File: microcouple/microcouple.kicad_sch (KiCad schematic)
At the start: 34 parts, among them J1 Conn_ARM_SWD_TagConnect_TC203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, J2 USB_C_Socket, SW1 ~{RESET}, U1 USBLC6-2SC6, U2 RP2040, X1 12MHz 12pF

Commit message: Finish Silkscreen
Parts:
- C1, C11, C8, C9: footprint Capacitor_SMD:C_0402_1005Metric -> GS_SMD:0402_1005Metric
- C10, C12, C19, C2, C24, C25, C26, C3, C4, C5, C6, C7: footprint Capacitor_SMD:C_0201_0603Metric -> GS_SMD:0201_0603Metric
- D1: footprint LED_SMD:LED_0201_0603Metric -> GS_Optoelectronics:LED_0201_0603Metric
- R1, R2, R3, R6, R7, R8: footprint Resistor_SMD:R_0201_0603Metric -> GS_SMD:0201_0603Metric
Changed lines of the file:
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@@
 			)
 		)
-		(property "Footprint" "Capacitor_SMD:C_0201_0603Metric"
+		(property "Footprint" "GS_SMD:0201_0603Metric"
 			(at 157.1752 36.83 0)
 			(effects
@@
 			)
 		)
-		(property "Footprint" "Resistor_SMD:R_0201_0603Metric"
+		(property "Footprint" "GS_SMD:0201_0603Metric"
 			(at 128.016 61.214 90)
 			(effects
@@
 			)
 		)
-		(property "Footprint" "Capacitor_SMD:C_0201_0603Metric"
+		(property "Footprint" "GS_SMD:0201_0603Metric"
 			(at 38.4048 147.32 0)
 			(effects
@@
 			)
 		)
-		(property "Footprint" "Capacitor_SMD:C_0402_1005Metric"
+		(property "Footprint" "GS_SMD:0402_1005Metric"
 			(at 244.8052 36.83 0)
 			(effects
@@
 			)
 		)
-		(property "Footprint" "Resistor_SMD:R_0201_0603Metric"
+		(property "Footprint" "GS_SMD:0201_0603Metric"
 			(at 218.186 61.214 90)
 			(effects
@@
 			)
 		)
-		(property "Footprint" "Capacitor_SMD:C_0201_0603Metric"
+		(property "Footprint" "GS_SMD:0201_0603Metric"
 			(at 171.1452 36.83 0)
 			(effects
@@
 			)
 		)
-		(property "Footprint" "Capacitor_SMD:C_0201_0603Metric"
+		(property "Footprint" "GS_SMD:0201_0603Metric"
 			(at 165.1 186.9948 0)
 			(effects
@@
 			)
 		)
-		(property "Footprint" "Resistor_SMD:R_0201_0603Metric"
+		(property "Footprint" "GS_SMD:0201_0603Metric"
 			(at 68.326 143.256 90)
 			(effects
@@
 			)
 		)
-		(property "Footprint" "Capacitor_SMD:C_0201_0603Metric"
+		(property "Footprint" "GS_SMD:0201_0603Metric"
 			(at 219.4052 36.83 0)
 			(effects
@@
 			)
 		)
-		(property "Footprint" "Capacitor_SMD:C_0201_0603Metric"
+		(property "Footprint" "GS_SMD:0201_0603Metric"
 			(at 103.8352 134.62 0)
 			(effects
@@
 			)
 		)
-		(property "Footprint" "Resistor_SMD:R_0201_0603Metric"
+		(property "Footprint" "GS_SMD:0201_0603Metric"
 			(at 208.026 61.214 90)
 			(effects
@@
 			)
 		)
-		(property "Footprint" "Capacitor_SMD:C_0201_0603Metric"
+		(property "Footprint" "GS_SMD:0201_0603Metric"
 			(at 119.38 186.9948 0)
 			(effects
@@
 			)
 		)
-		(property "Footprint" "Capacitor_SMD:C_0201_0603Metric"
+		(property "Footprint" "GS_SMD:0201_0603Metric"
 			(at 143.2052 36.83 0)
 			(effects
@@
 			)
 		)
-		(property "Footprint" "Capacitor_SMD:C_0201_0603Metric"
+		(property "Footprint" "GS_SMD:0201_0603Metric"
 			(at 82.2452 134.62 0)
 			(effects
@@
 			)
 		)
-		(property "Footprint" "Capacitor_SMD:C_0201_0603Metric"
+		(property "Footprint" "GS_SMD:0201_0603Metric"
 			(at 270.2052 36.83 0)
 			(effects
@@
 			)
 		)
-		(property "Footprint" "Resistor_SMD:R_0201_0603Metric"
+		(property "Footprint" "GS_SMD:0201_0603Metric"
 			(at 87.376 39.624 90)
 			(effects
@@
 			)
 		)
-		(property "Footprint" "Resistor_SMD:R_0201_0603Metric"
+		(property "Footprint" "GS_SMD:0201_0603Metric"
 			(at 59.944 143.764 90)
 			(effects
@@
 			)
 		)
-		(property "Footprint" "Capacitor_SMD:C_0201_0603Metric"
+		(property "Footprint" "GS_SMD:0201_0603Metric"
 			(at 129.2352 36.83 0)
 			(effects
@@
 			)
 		)
-		(property "Footprint" "Capacitor_SMD:C_0201_0603Metric"
+		(property "Footprint" "GS_SMD:0201_0603Metric"
 			(at 143.51 186.9948 0)
 			(effects
@@
 			)
 		)
-		(property "Footprint" "Capacitor_SMD:C_0402_1005Metric"
+		(property "Footprint" "GS_SMD:0402_1005Metric"
 			(at 115.2652 36.83 0)
 			(effects
@@
 			)
 		)
-		(property "Footprint" "Capacitor_SMD:C_0402_1005Metric"
+		(property "Footprint" "GS_SMD:0402_1005Metric"
 			(at 28.2448 69.85 0)
 			(effects
@@
 			)
 		)
-		(property "Footprint" "Capacitor_SMD:C_0402_1005Metric"
+		(property "Footprint" "GS_SMD:0402_1005Metric"
 			(at 194.0052 36.83 0)
 			(effects
@@
 			)
 		)
-		(property "Footprint" "LED_SMD:LED_0201_0603Metric"
+		(property "Footprint" "GS_Optoelectronics:LED_0201_0603Metric"
 			(at 86.36 31.75 0)
 			(effects

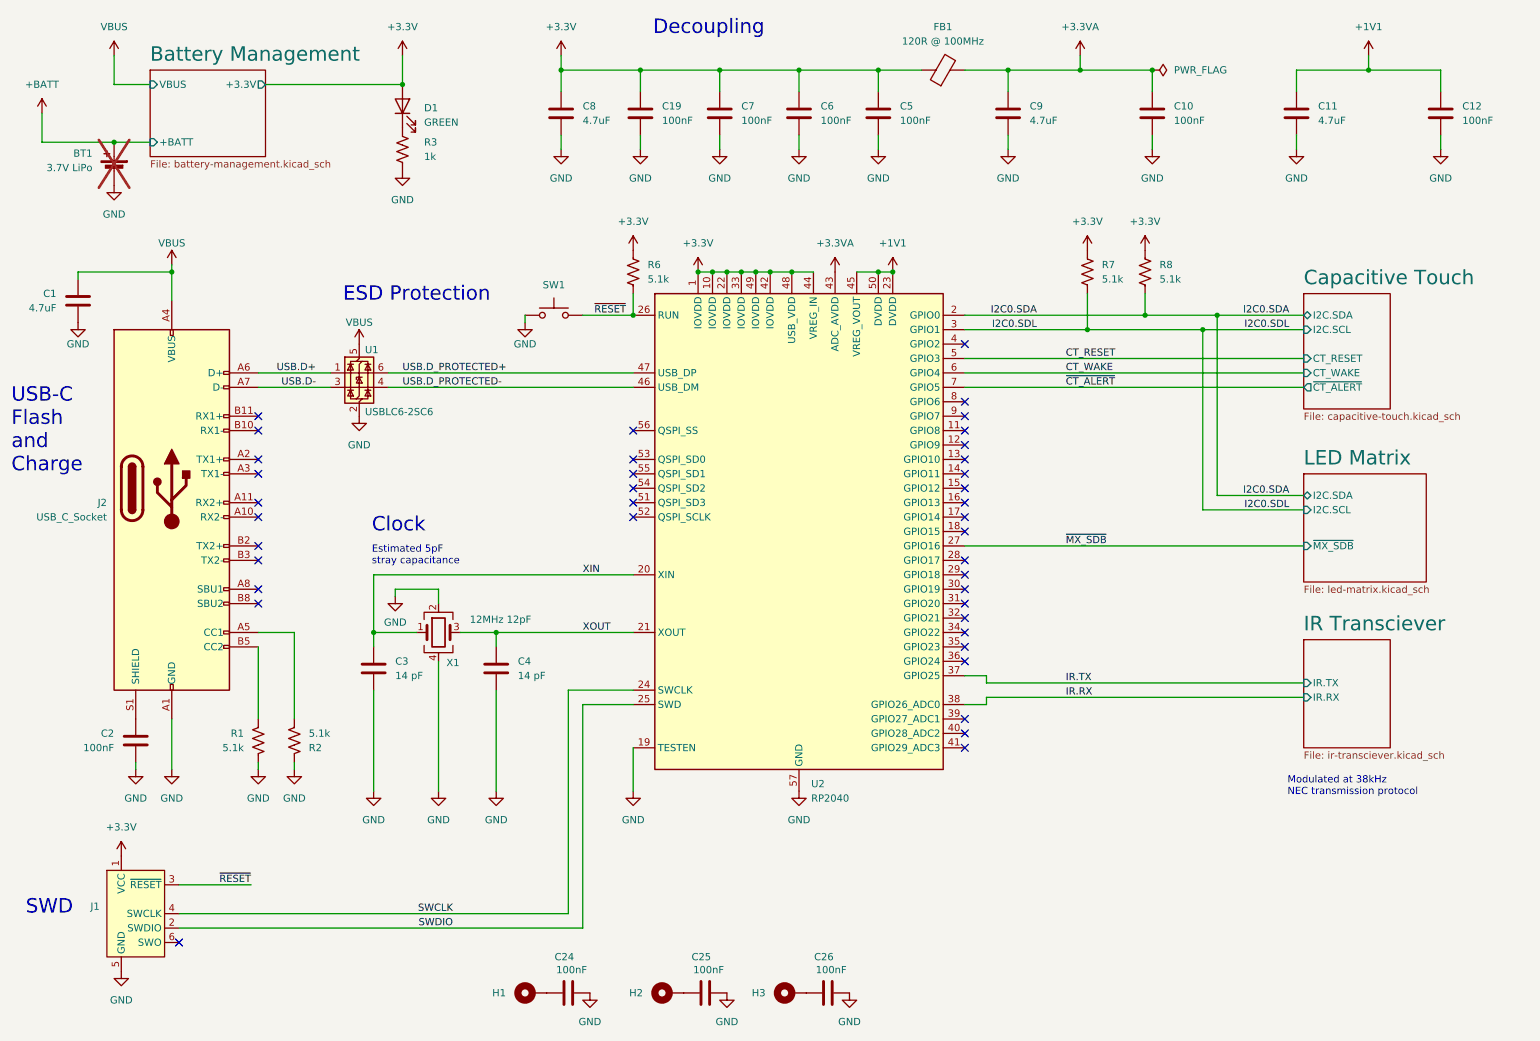
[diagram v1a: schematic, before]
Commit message: Update for JLCPCB
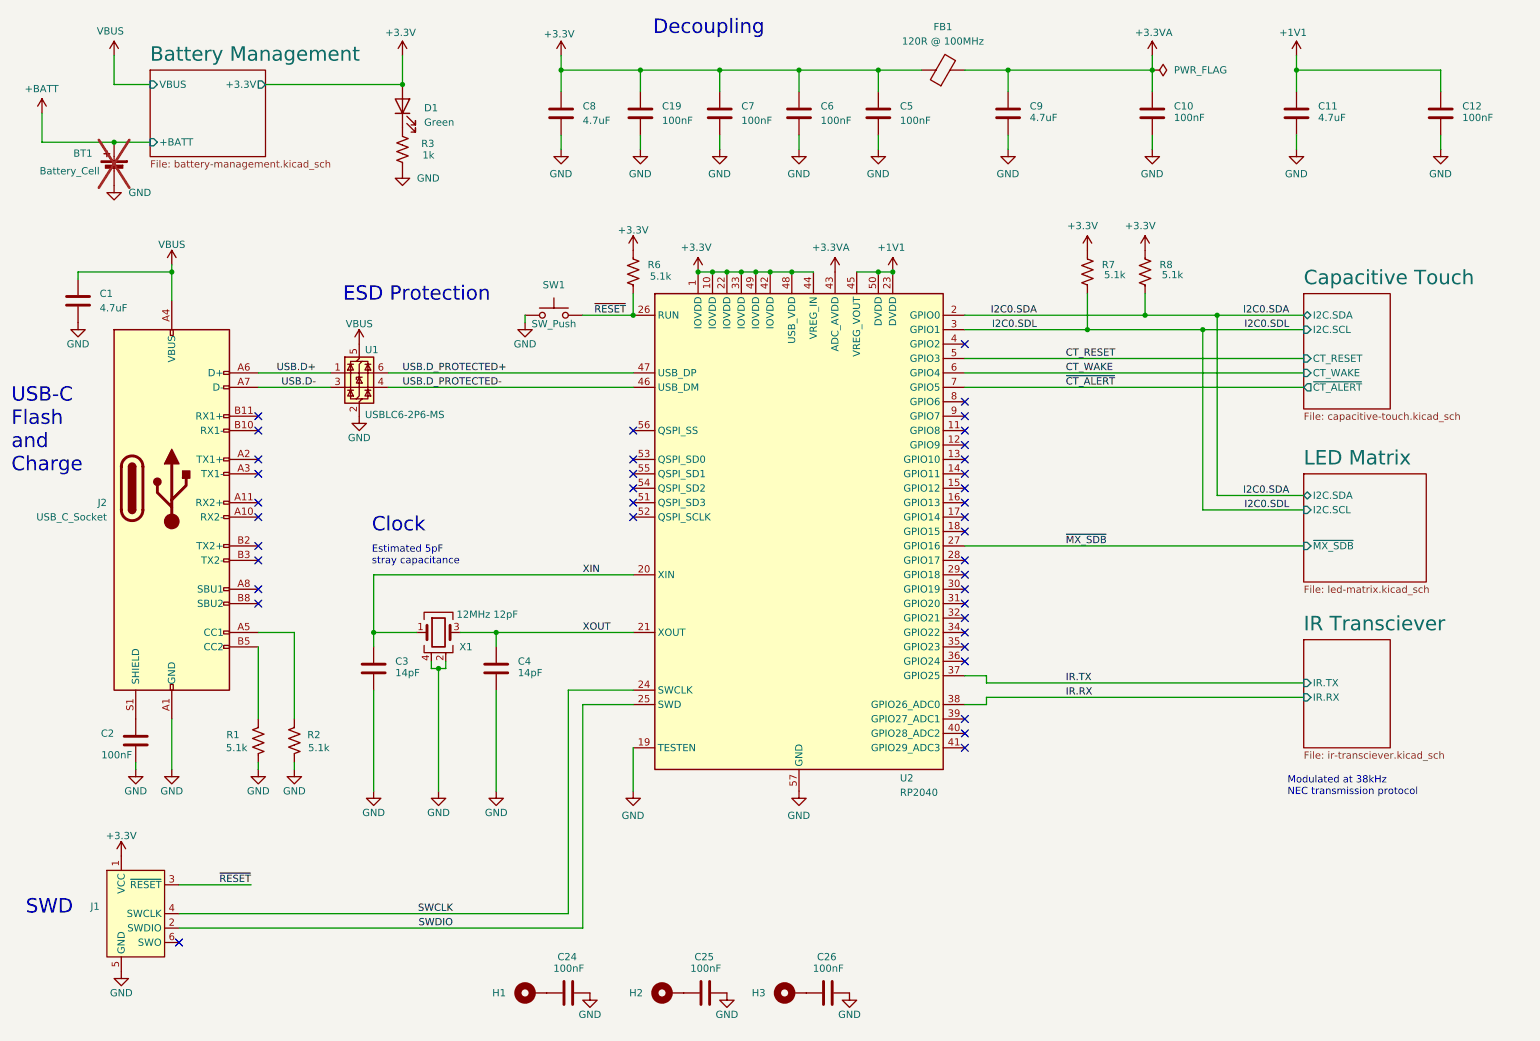
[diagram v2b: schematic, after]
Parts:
- BT1: value 3.7V LiPo -> Battery_Cell
- C1, C11, C8, C9: footprint GS_SMD:0402_1005Metric -> GS_Capacitors:C_0402_1005Metric; symbol Device:C -> GS_Capacitor_0402:C_0402_4.7uF; LCSC ID (none) -> C76996; Manufacturer (none) -> Murata Electronics; Mfr. Part # (none) -> GRM155R60J475ME87D; Package (none) -> 0402
- C10, C12, C19, C2, C24, C25, C26, C5, C6, C7: footprint GS_SMD:0201_0603Metric -> GS_Capacitors:C_0201_0603Metric; symbol Device:C -> GS_Capacitor_0201:C_0201_100nF; LCSC ID (none) -> C18164587; Manufacturer (none) -> CCTC; Mfr. Part # (none) -> TCC0201X5R104M250ZT; Package (none) -> 0201
- C3, C4: value 14 pF -> 14pF; footprint GS_SMD:0201_0603Metric -> GS_Capacitors:C_0201_0603Metric; symbol Device:C -> GS_Capacitor_0201:C_0201_14pF; LCSC ID (none) -> C3037637; Manufacturer (none) -> FH (Guangdong Fenghua Advanced Tech); Mfr. Part # (none) -> 0201CG140J500NT; Package (none) -> 0201
- D1: value GREEN -> Green; symbol Device:LED -> GS_Optoelectronic:LED_0201_Green; LCSC ID (none) -> C3646922; Manufacturer (none) -> XINGLIGHT; Mfr. Part # (none) -> XL-0201UGC; Package (none) -> 0201
- FB1: footprint Inductor_SMD:L_0805_2012Metric_Pad1.15x1.40mm_HandSolder -> Inductor_SMD:L_0805_2012Metric; symbol Device:FerriteBead -> GS_Inductors:FB_0805_120R; LCSC ID (none) -> C356987; Manufacturer (none) -> TAI-TECH; Mfr. Part # (none) -> HCB2012KF-121T30; Package (none) -> 0805
- J2: Manufacturer (none) -> SHOU HAN; Mfr. Part # (none) -> TYPE-C 24P QT; Package (none) -> SMD
- R1, R2, R6, R7, R8: footprint GS_SMD:0201_0603Metric -> GS_Resistors:R_0201_0603Metric; symbol Device:R_US -> GS_Resistor_0201:R_0201_5.1k; LCSC ID (none) -> C158467; Manufacturer (none) -> RALEC; Mfr. Part # (none) -> RTT01512JTH; Package (none) -> 0201
- R3: footprint GS_SMD:0201_0603Metric -> GS_Resistors:R_0201_0603Metric; symbol Device:R_US -> GS_Resistor_0201:R_0201_1k; LCSC ID (none) -> C304503; Manufacturer (none) -> FH (Guangdong Fenghua Advanced Tech); Mfr. Part # (none) -> RC-01W102JT; Package (none) -> 0201
- SW1: value ~{RESET} -> SW_Push; symbol Switch:SW_Push -> GS_Switches:SW_Push_B3U-1000P; LCSC ID (none) -> C231329; Manufacturer (none) -> Omron Electronics; Mfr. Part # (none) -> B3U-1000P; Package (none) -> SMD, 2.5x3mm
- U1: value USBLC6-2SC6 -> USBLC6-2P6-MS; footprint Package_TO_SOT_SMD:SOT-23-6 -> Package_TO_SOT_SMD:SOT-666; symbol Power_Protection:USBLC6-2SC6 -> GS_IC:USBLC6-2P6-MS; LCSC ID (none) -> C3647099; Manufacturer (none) -> MSKSEMI; Mfr. Part # (none) -> USBLC6-2P6-MS; Package (none) -> SOT-666
- U2: LCSC ID (none) -> C2040; Manufacturer (none) -> Raspberry Pi; Mfr. Part # (none) -> RP2040; Package (none) -> LQFN-56(7x7)
- X1: symbol Device:Crystal_GND24 -> GS_Oscillators:Crystal_3225_12MHz; Manufacturer (none) -> Yajingxin; Mfr. Part # (none) -> TAXM12M4RFBCCT2T; Package (none) -> SMD3225-4P
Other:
- moved on the sheet: X1
